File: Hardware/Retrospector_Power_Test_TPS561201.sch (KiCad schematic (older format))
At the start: 21 parts, among them J2 Eurorack_10_pin_power, U1 LM2675M-ADJ, U2 LD1117-3.3-4Tab

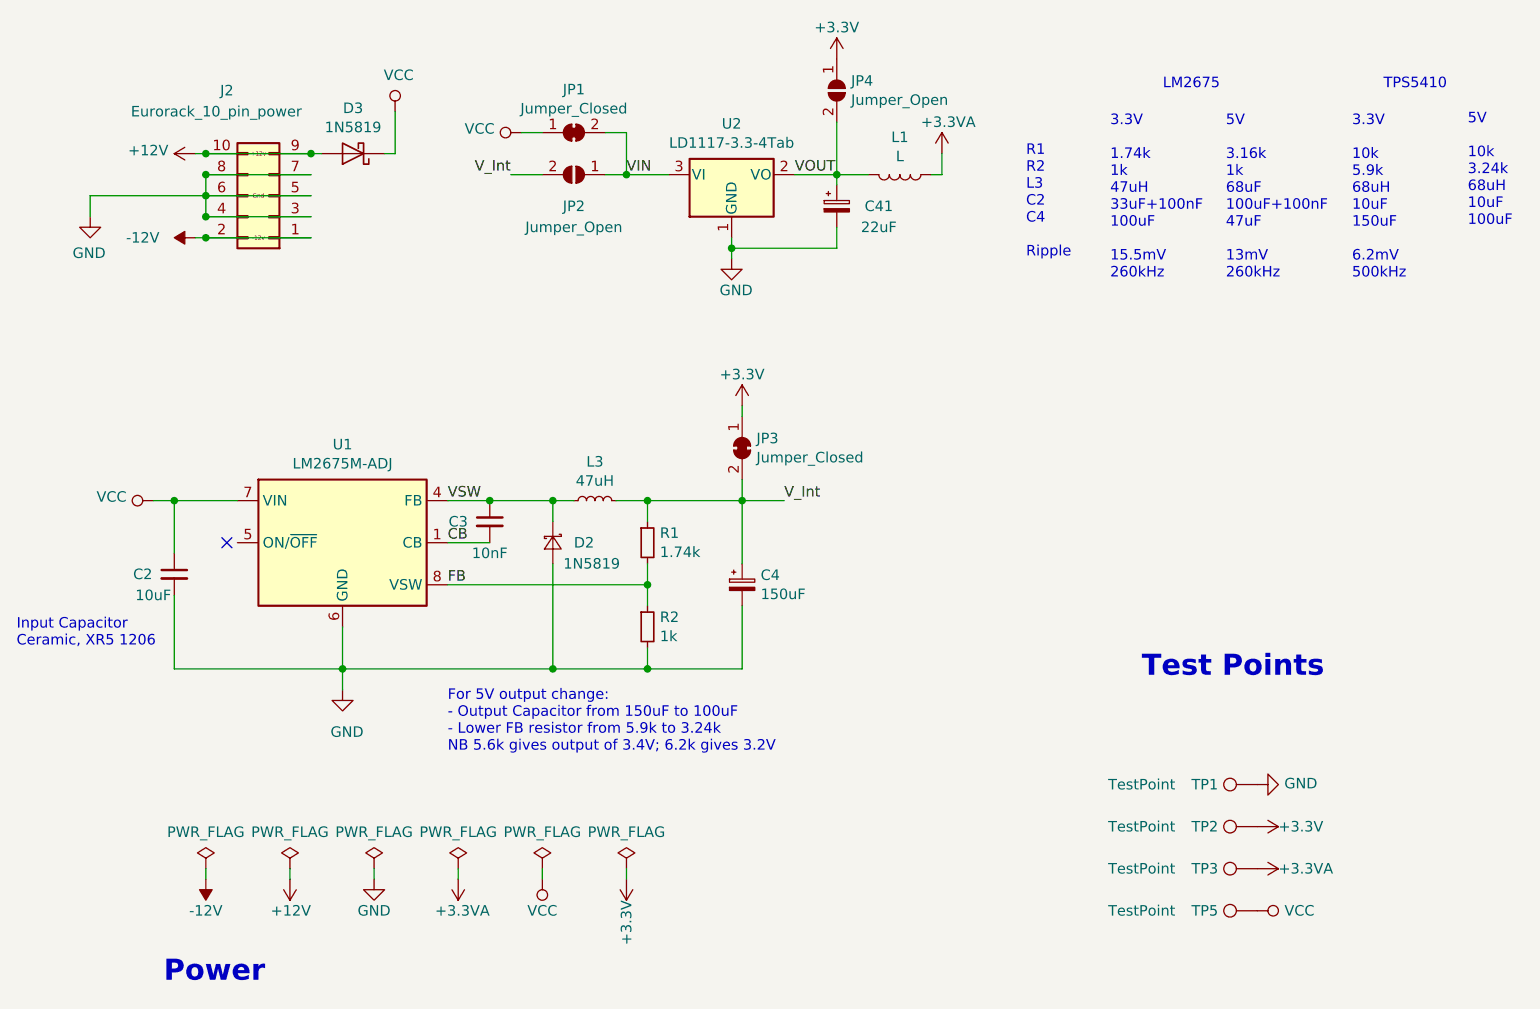
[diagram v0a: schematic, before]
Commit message: Power test PCBs finished and sent to production; basic implementation of clocked delay
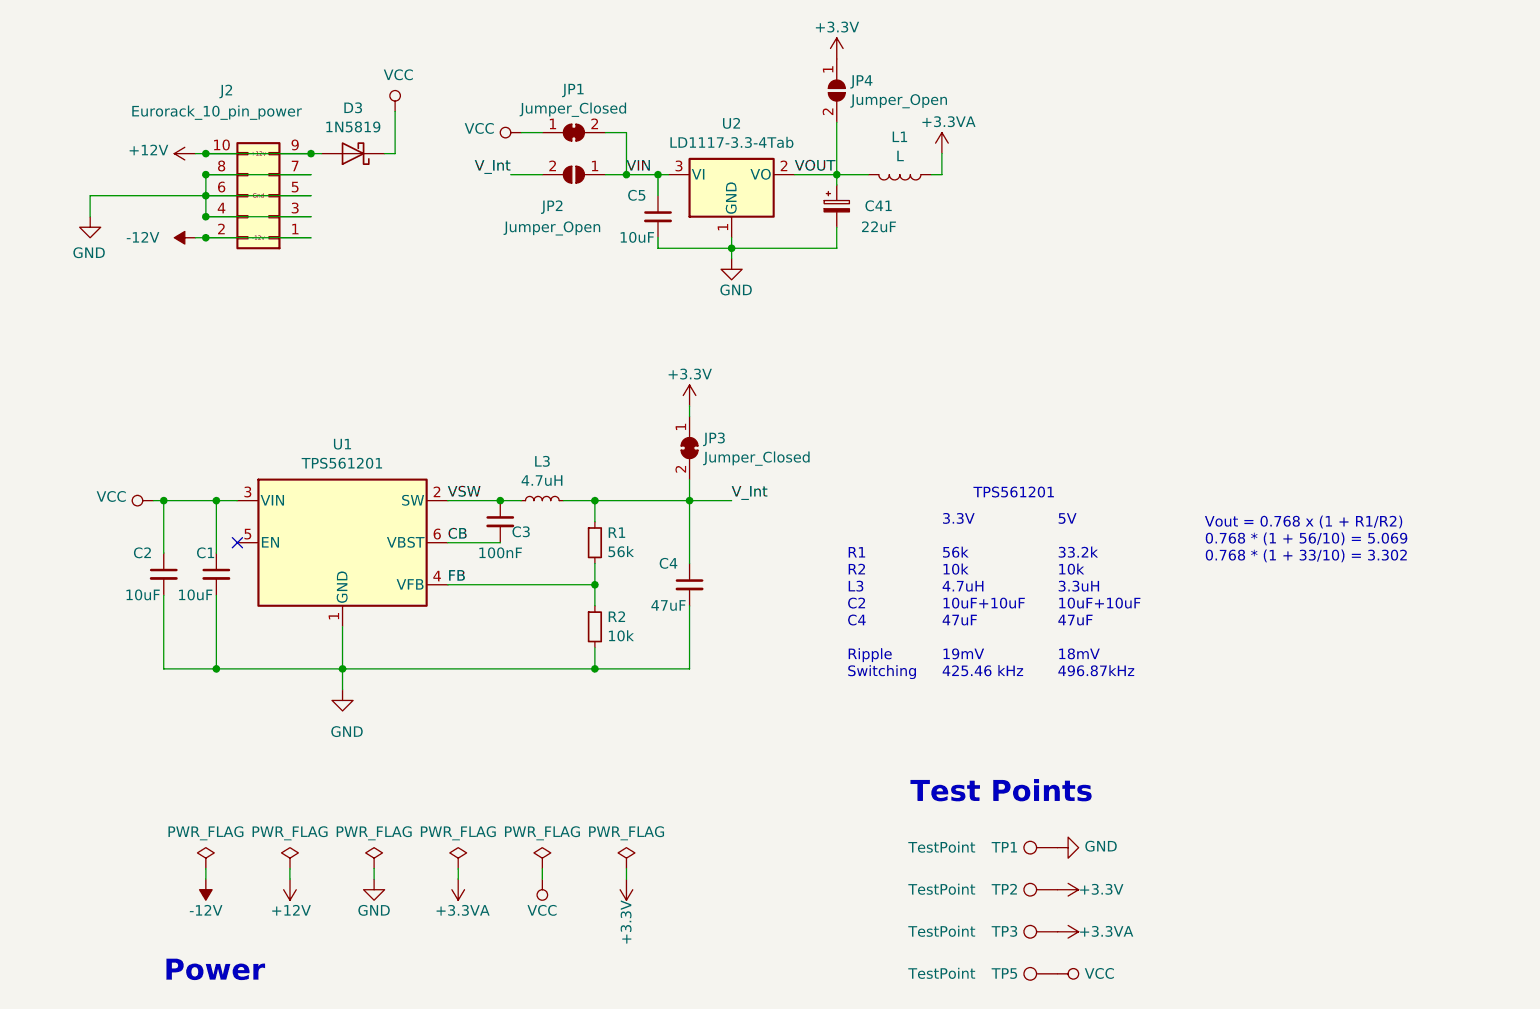
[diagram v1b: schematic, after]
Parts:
- removed C4: 150uF, Capacitors_SMD:C_1210, symbol Device:CP_Small
- removed D2: 1N5819, Diodes_SMD:D_SOD-123, symbol Device:D_Schottky_Small
- removed U1: LM2675M-ADJ, Housings_SOIC:SOIC-8_3.9x4.9mm_Pitch1.27mm, symbol LM2675M-ADJ:LM2675M-ADJ
- added C1, C5: 10uF, Resistors_SMD:R_0805, symbol Device:C_Small
- added C4: 47uF, Resistors_SMD:R_1206, symbol Device:C_Small
- added U1: TPS561201, TO_SOT_Packages_SMD:SOT-23-6_Handsoldering, symbol TPS561201:TPS561201
- C2: footprint Capacitors_SMD:C_1210 -> Resistors_SMD:R_0805
- C3: value 10nF -> 100nF; footprint Capacitors_SMD:C_0603_HandSoldering -> Resistors_SMD:R_0805
- L3: value 47uH -> 4.7uH; footprint Inductors_SMD:L_6.3x6.3_H3 -> Custom_Footprints:L_0806
- R1: value 1.74k -> 56k
- R2: value 1k -> 10k
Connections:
- net CB: now also U1.6 (VBST)
- net FB: now also U1.4 (VFB)
- net GND: now also C1.2, C4.2, C5.2, U1.1 (GND)
- net VCC: now also C1.1, U1.3 (VIN)
- net VIN: now also C5.1
- net VSW: now also U1.2 (SW)
- net V_Int: now also C4.1
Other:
- note added: "3.3V\n\n56k\n10k\n4.7uH\n10uF+10uF\n47uF\n\n19mV\n425.46 kHz"
- note added: "5V\n\n33.2k\n10k\n3.3uH\n10uF+10uF\n47uF\n\n18mV\n496.87kHz"
- note added: "R1\nR2\nL3\nC2\nC4\n\nRipple\nSwitching"
- note added: "TPS561201"
- note added: "Vout = 0.768 x (1 + R1/R2)\n0.768 * (1 + 56/10) = 5.069\n0.768 * (1 + 33/10) = 3.302"
- note removed: "3.3V\n\n1.74k\n1k\n47uH\n33uF+100nF\n100uF\n\n15.5mV\n260kHz"
- note removed: "3.3V\n\n10k\n5.9k\n68uH\n10uF\n150uF\n\n6.2mV\n500kHz"
- note removed: "5V\n\n10k\n3.24k\n68uH\n10uF\n100uF"
- note removed: "5V\n\n3.16k\n1k\n68uF\n100uF+100nF\n47uF\n\n13mV\n260kHz"
- note removed: "For 5V output change:\n- Output Capacitor from 150uF to 100uF\n- Lower FB resistor from 5.9k to 3.24k\nNB 5.6k gives output of 3.4V; 6.2k gives 3.2V"
- note removed: "Input Capacitor\nCeramic, XR5 1206"
- note removed: "LM2675"
- note removed: "R1\nR2\nL3\nC2\nC4\n\nRipple"
- note removed: "TPS5410"
- moved on the sheet: C2, C3, JP3, L3, R1, R2, TP1, TP2, TP3, TP5

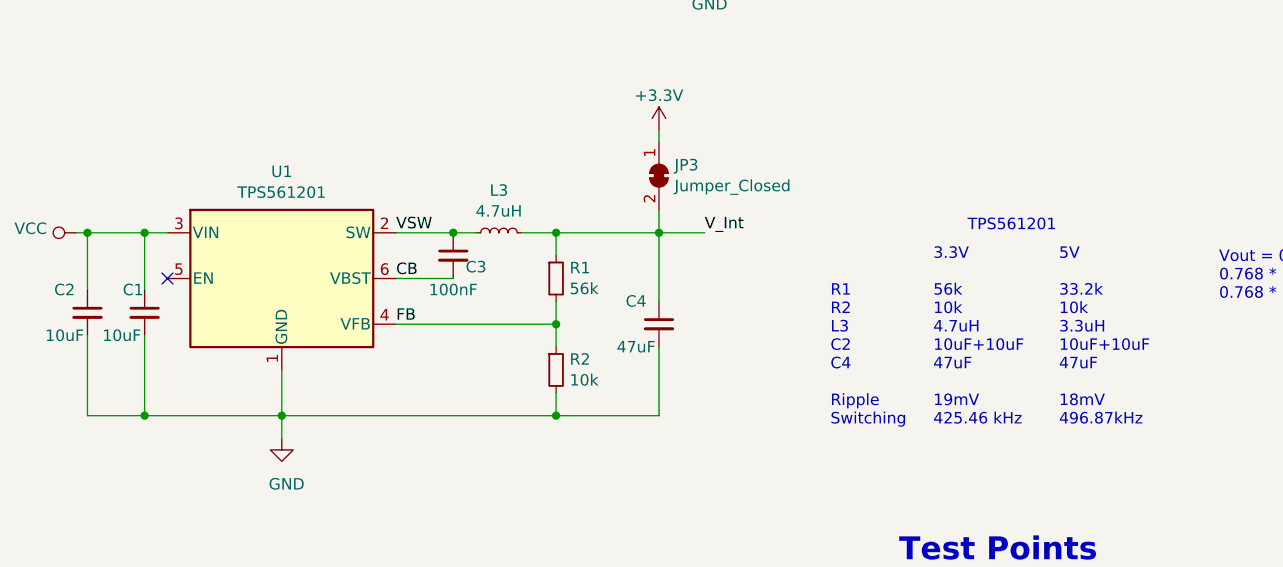
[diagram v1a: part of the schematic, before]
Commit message: Debugging DAC clock issues when using FMC to control SDRAM
Workaround is to switch the clock for the I2S DAC to peripheral clock (also used by ADC at present)
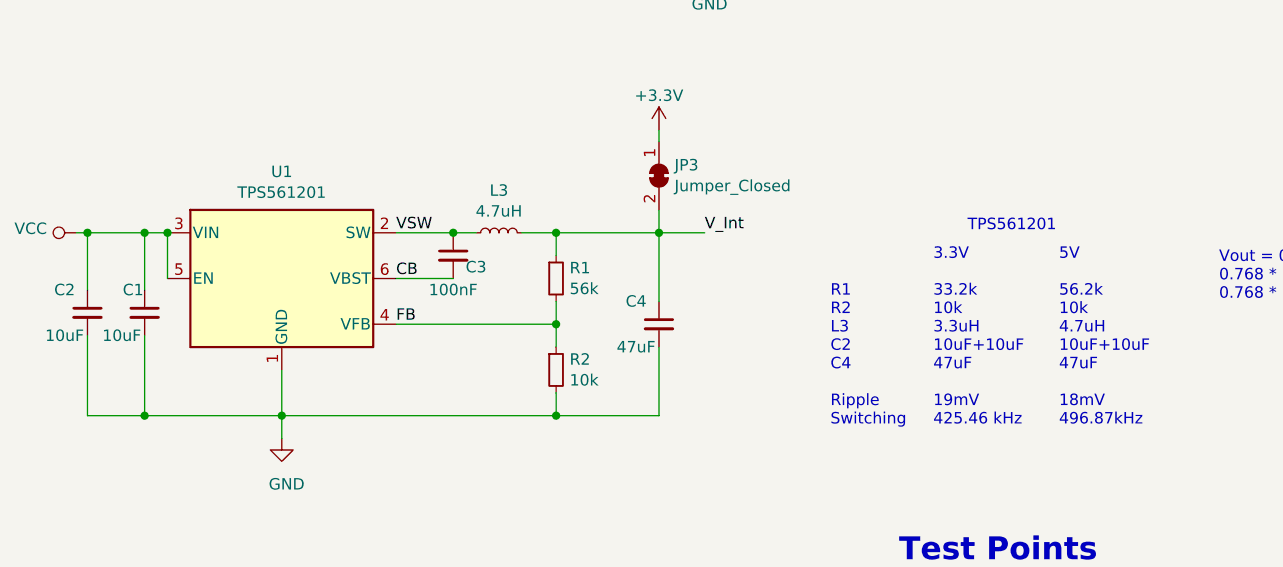
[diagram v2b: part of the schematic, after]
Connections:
- net VCC: now also U1.5 (EN)
- no-connect marks 1 -> 0
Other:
- note added: "3.3V\n\n33.2k\n10k\n3.3uH\n10uF+10uF\n47uF\n\n19mV\n425.46 kHz"
- note added: "5V\n\n56.2k\n10k\n4.7uH\n10uF+10uF\n47uF\n\n18mV\n496.87kHz"
- note removed: "3.3V\n\n56k\n10k\n4.7uH\n10uF+10uF\n47uF\n\n19mV\n425.46 kHz"
- note removed: "5V\n\n33.2k\n10k\n3.3uH\n10uF+10uF\n47uF\n\n18mV\n496.87kHz"
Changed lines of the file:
@@
 Wire Wire Line
 	2600 3150 2850 3150
-NoConn ~ 1600 3150
 $Comp
 L power:GND #PWR03
@@
 TPS561201
 Text Notes 4950 3800 0    50   ~ 0
-3.3V\n\n56k\n10k\n4.7uH\n10uF+10uF\n47uF\n\n19mV\n425.46 kHz
+3.3V\n\n33.2k\n10k\n3.3uH\n10uF+10uF\n47uF\n\n19mV\n425.46 kHz
 $Comp
 L TPS561201:TPS561201 U1
@@
 Connection ~ 1500 3750
 Text Notes 5500 3800 0    50   ~ 0
-5V\n\n33.2k\n10k\n3.3uH\n10uF+10uF\n47uF\n\n18mV\n496.87kHz
+5V\n\n56.2k\n10k\n4.7uH\n10uF+10uF\n47uF\n\n18mV\n496.87kHz
 Wire Wire Line
 	2100 3750 3300 3750
@@
 Wire Wire Line
 	3600 1750 3950 1750
+Wire Wire Line
+	1600 3150 1600 2950
+Connection ~ 1600 2950
 $EndSCHEMATC
